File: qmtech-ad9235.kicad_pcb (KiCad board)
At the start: 4 copper layers, 55 x 75 mm, 58 parts

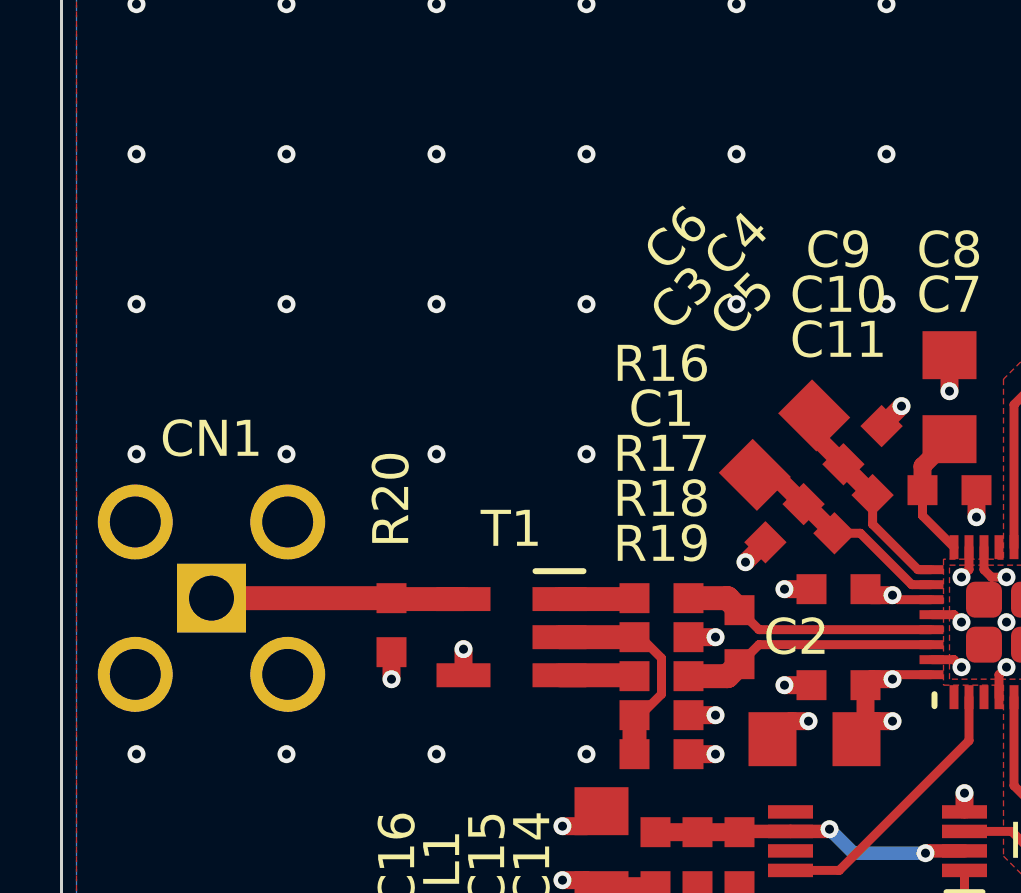
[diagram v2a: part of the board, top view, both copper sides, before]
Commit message: simplify input circuit in qmtech-ad9235
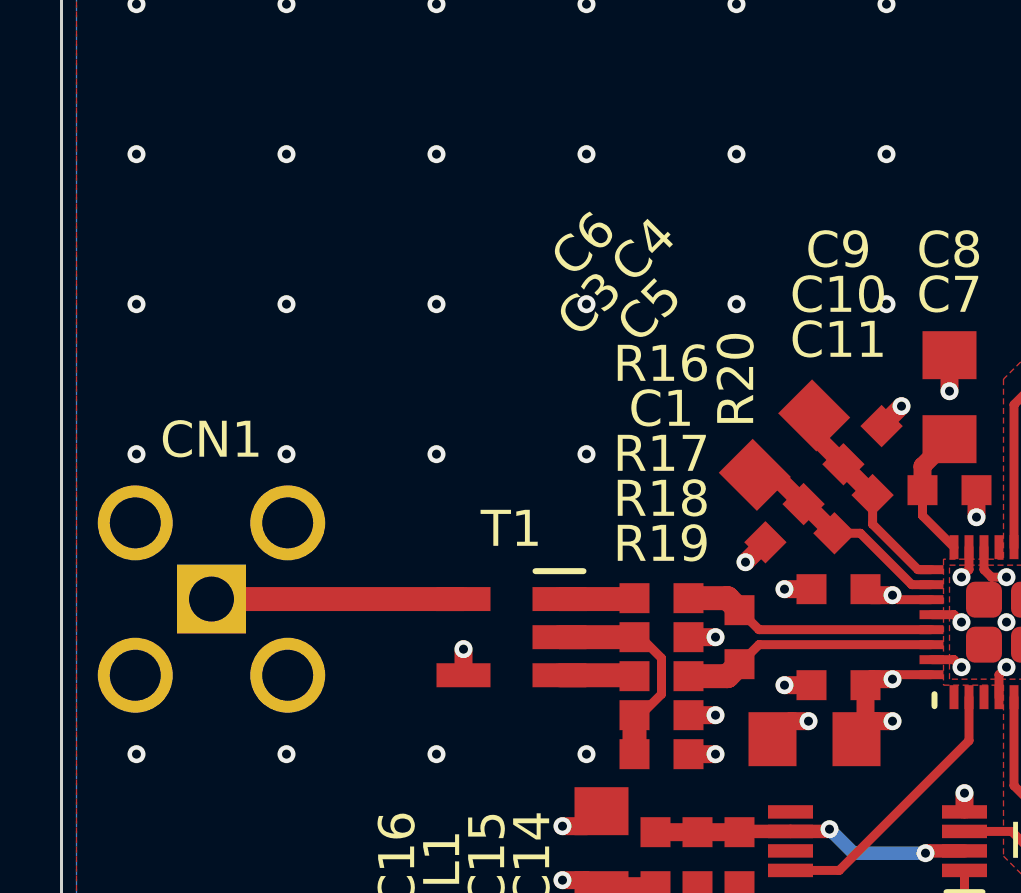
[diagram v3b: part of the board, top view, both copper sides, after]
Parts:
- removed C2: , footprints:0603
- moved R20 11.6 mm to (142.6, 83.6)
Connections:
- R20 pad 1: INPUT -> VIN+
- R20 pad 2: GND -> VIN-
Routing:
- net GND: track 42.1 -> 41.2 mm, vias 138 -> 137
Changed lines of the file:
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@@
     (pad "" np_thru_hole circle (at 0 0) (size 3.2 3.2) (drill 3.2) (layers "*.Cu" "*.Mask"))
-  )
-  (footprint "footprints:0603" (layer "F.Cu")
-    (at 142.6 83.6 -90)
-    (property "mpn" "C1648")
-    (attr smd)
-    (fp_text reference "C2" (at 0 -1.9 -180) (layer "F.SilkS")
-        (effects (font (size 1.2 1.2) (thickness 0.2)))
-    )
-    (fp_text value "" (at 0 0 -90) (layer "F.SilkS")
-        (effects (font (size 1.27 1.27) (thickness 0.15)))
-    )
-    (fp_text user "${REFERENCE}" (at 0 -1.9 -180) (layer "F.Fab")
-        (effects (font (size 1.2 1.2) (thickness 0.2)))
-    )
-    (pad "1" smd rect (at -0.9 0 270) (size 1 1) (layers "F.Cu" "F.Paste" "F.Mask")
-      (net 35 "VIN+"))
-    (pad "2" smd rect (at 0.9 0 270) (size 1 1) (layers "F.Cu" "F.Paste" "F.Mask")
-      (net 36 "VIN-"))
   )
   (footprint "footprints:1206" (layer "F.Cu")
@@
     (property "mpn" "C14663")
     (attr smd)
-    (fp_text reference "C4" (at 1.767768 -7.707463 45) (layer "F.SilkS")
+    (fp_text reference "C4" (at -0.565685 -9.758073 45) (layer "F.SilkS")
         (effects (font (size 1.2 1.2) (thickness 0.2)))
     )
@@
         (effects (font (size 1.27 1.27) (thickness 0.15)))
     )
-    (fp_text user "${REFERENCE}" (at 1.767768 -7.707463 45) (layer "F.Fab")
+    (fp_text user "${REFERENCE}" (at -0.565685 -9.758073 45) (layer "F.Fab")
         (effects (font (size 1.2 1.2) (thickness 0.2)))
     )
@@
   )
   (footprint "footprints:SMA" (layer "F.Cu")
-    (at 125 82.3)
+    (at 125 82.33)
     (property "mpn" "C914554")
     (attr through_hole)
@@
   (footprint "footprints:0603" (layer "F.Cu")
     (at 166.5 105.18)
-    (property "mpn" "C8218")
+    (property "mpn" "C22962")
     (attr smd)
     (fp_text reference "R23" (at -4 0) (layer "F.SilkS")
@@
     (property "mpn" "C14663")
     (attr smd)
-    (fp_text reference "C5" (at 2.333452 -7.566043 45) (layer "F.SilkS")
+    (fp_text reference "C5" (at -0.000001 -9.616653 45) (layer "F.SilkS")
         (effects (font (size 1.2 1.2) (thickness 0.2)))
     )
@@
         (effects (font (size 1.27 1.27) (thickness 0.15)))
     )
-    (fp_text user "${REFERENCE}" (at 2.333452 -7.566043 45) (layer "F.Fab")
+    (fp_text user "${REFERENCE}" (at -0.000001 -9.616653 45) (layer "F.Fab")
         (effects (font (size 1.2 1.2) (thickness 0.2)))
     )
@@
   (footprint "footprints:0603" (layer "F.Cu")
     (at 140 82.3)
-    (property "mpn" "C23140")
+    (property "mpn" "C23345")
     (attr smd)
     (fp_text reference "R16" (at 0 -7.8) (layer "F.SilkS")
@@
     (property "mpn" "C14663")
     (attr smd)
-    (fp_text reference "C3" (at -2.899137 7.707463 -135) (layer "F.SilkS")
+    (fp_text reference "C3" (at -0.565685 9.758073 -135) (layer "F.SilkS")
         (effects (font (size 1.2 1.2) (thickness 0.2)))
     )
@@
         (effects (font (size 1.27 1.27) (thickness 0.15)))
     )
-    (fp_text user "${REFERENCE}" (at -2.899137 7.707463 -135) (layer "F.Fab")
+    (fp_text user "${REFERENCE}" (at -0.565685 9.758073 -135) (layer "F.Fab")
         (effects (font (size 1.2 1.2) (thickness 0.2)))
     )
@@
     (property "mpn" "C13585")
     (attr smd)
-    (fp_text reference "C6" (at 2.333452 -7.424621 45) (layer "F.SilkS")
+    (fp_text reference "C6" (at 0 -9.475231 45) (layer "F.SilkS")
         (effects (font (size 1.2 1.2) (thickness 0.2)))
     )
@@
         (effects (font (size 1.27 1.27) (thickness 0.15)))
     )
-    (fp_text user "${REFERENCE}" (at 2.333452 -7.424621 45) (layer "F.Fab")
+    (fp_text user "${REFERENCE}" (at 0 -9.475231 45) (layer "F.Fab")
         (effects (font (size 1.2 1.2) (thickness 0.2)))
     )
@@
   (footprint "footprints:0603" (layer "F.Cu")
     (at 140 84.9)
-    (property "mpn" "C23140")
+    (property "mpn" "C23345")
     (attr smd)
     (fp_text reference "R17" (at 0 -7.4) (layer "F.SilkS")
@@
   )
   (footprint "footprints:0603" (layer "F.Cu")
-    (at 131 83.2 -90)
-    (property "mpn" "C23185")
-    (attr smd)
-    (fp_text reference "R20" (at -4.2 0 -90) (layer "F.SilkS")
+    (at 142.6 83.6 -90)
+    (property "mpn" "C22962")
+    (attr smd)
+    (fp_text reference "R20" (at -8.6 0.1 90) (layer "F.SilkS")
         (effects (font (size 1.2 1.2) (thickness 0.2)))
     )
@@
         (effects (font (size 1.27 1.27) (thickness 0.15)))
     )
-    (fp_text user "${REFERENCE}" (at -4.2 0 -90) (layer "F.Fab")
+    (fp_text user "${REFERENCE}" (at -8.6 0.1 90) (layer "F.Fab")
         (effects (font (size 1.2 1.2) (thickness 0.2)))
     )
     (pad "1" smd rect (at -0.9 0 270) (size 1 1) (layers "F.Cu" "F.Paste" "F.Mask")
-      (net 40 "INPUT"))
+      (net 35 "VIN+"))
     (pad "2" smd rect (at 0.9 0 270) (size 1 1) (layers "F.Cu" "F.Paste" "F.Mask")
-      (net 18 "GND"))
+      (net 36 "VIN-"))
   )
   (footprint "footprints:SOT23" (layer "F.Cu")
@@
   (footprint "footprints:0603" (layer "F.Cu")
     (at 166.5 110.26)
-    (property "mpn" "C8218")
+    (property "mpn" "C22962")
     (attr smd)
     (fp_text reference "R21" (at -4 0) (layer "F.SilkS")
@@
   (footprint "footprints:0603" (layer "F.Cu")
     (at 166.5 107.72)
-    (property "mpn" "C8218")
+    (property "mpn" "C22962")
     (attr smd)
     (fp_text reference "R22" (at -4 0) (layer "F.SilkS")
@@
   (segment (start 144.1 82) (end 145 82) (width 0.6) (layer "F.Cu") (net 18))
   (segment (start 151.25 85.6) (end 151.25 84.85) (width 0.3) (layer "F.Cu") (net 18))
-  (segment (start 131 85) (end 131 84.1) (width 0.6) (layer "F.Cu") (net 18))
   (segment (start 148 75.9) (end 147.336396 76.563604) (width 0.6) (layer "F.Cu") (net 18))
   (segment (start 133.4 106) (end 133.9 105.5) (width 0.6) (layer "F.Cu") (net 18))
@@
   (via (at 141.8 83.6) (size 0.6) (drill 0.3) (layers "F.Cu" "B.Cu") (free) (net 18))
   (via (at 137.5 127.5) (size 0.6) (drill 0.3) (layers "F.Cu" "B.Cu") (free) (net 18))
-  (via (at 131 85) (size 0.6) (drill 0.3) (layers "F.Cu" "B.Cu") (free) (net 18))
   (via (at 127.5 67.5) (size 0.6) (drill 0.3) (layers "F.Cu" "B.Cu") (free) (net 18))
   (via (at 157.5 127.5) (size 0.6) (drill 0.3) (layers "F.Cu" "B.Cu") (free) (net 18))
@@
   (segment (start 139.07 82.33) (end 139.1 82.3) (width 0.8) (layer "F.Cu") (net 39))
   (segment (start 136.6 82.33) (end 139.07 82.33) (width 0.8) (layer "F.Cu") (net 39))
-  (segment (start 133.4 82.33) (end 131.03 82.33) (width 0.8) (layer "F.Cu") (net 40))
-  (segment (start 125 82.3) (end 131 82.3) (width 0.8) (layer "F.Cu") (net 40))
-  (segment (start 131.03 82.33) (end 131 82.3) (width 0.8) (layer "F.Cu") (net 40))
+  (segment (start 133.4 82.33) (end 125 82.33) (width 0.8) (layer "F.Cu") (net 40))
   (segment (start 143.110051 78.189949) (end 143.762741 78.189949) (width 0.6) (layer "F.Cu") (net 41))
   (segment (start 146.62929 80.136396) (end 145.763604 80.136396) (width 0.3) (layer "F.Cu") (net 41))

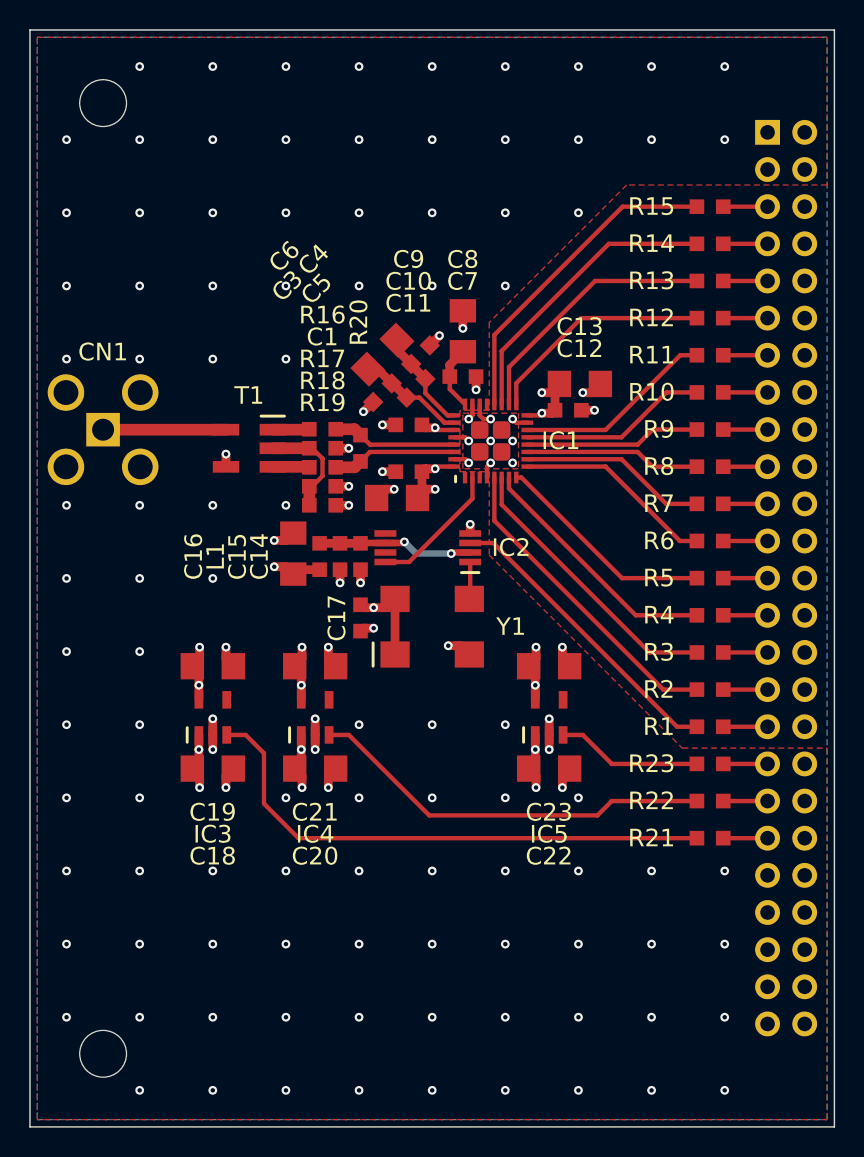
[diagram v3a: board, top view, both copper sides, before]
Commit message: update numbers in capacitor reference designators in qmtech-ad9235
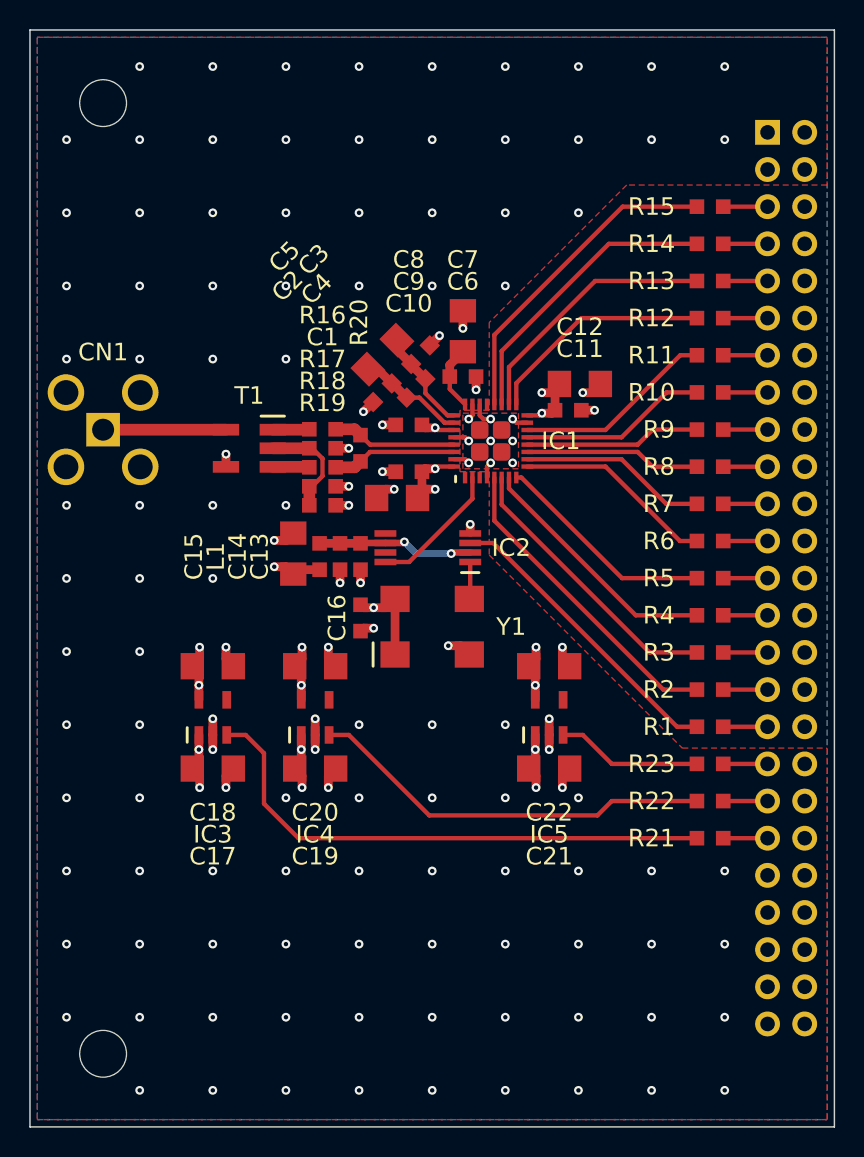
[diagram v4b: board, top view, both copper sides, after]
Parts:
- renumbered C11 to C10, C12 to C11, C13 to C12, C14 to C13, C15 to C14, C16 to C15, C17 to C16, C18 to C17, C19 to C18, C20 to C19, C3 to C2, C21 to C20, C22 to C21, C23 to C22, C4 to C3, C5 to C4, C6 to C5, C7 to C6, C8 to C7, C9 to C8, C10 to C9
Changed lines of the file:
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@@
     (property "mpn" "C14663")
     (attr smd)
-    (fp_text reference "C9" (at 0 11.3) (layer "F.SilkS")
+    (fp_text reference "C8" (at 0 11.3) (layer "F.SilkS")
         (effects (font (size 1.2 1.2) (thickness 0.2)))
     )
@@
     (property "mpn" "C14663")
     (attr smd)
-    (fp_text reference "C17" (at 0 1.6 90) (layer "F.SilkS")
+    (fp_text reference "C16" (at 0 1.6 90) (layer "F.SilkS")
         (effects (font (size 1.2 1.2) (thickness 0.2)))
     )
@@
     (property "mpn" "C13585")
     (attr smd)
-    (fp_text reference "C19" (at 0 10) (layer "F.SilkS")
+    (fp_text reference "C18" (at 0 10) (layer "F.SilkS")
         (effects (font (size 1.2 1.2) (thickness 0.2)))
     )
@@
     (property "mpn" "C14663")
     (attr smd)
-    (fp_text reference "C4" (at -0.565685 -9.758073 45) (layer "F.SilkS")
+    (fp_text reference "C3" (at -0.565685 -9.758073 45) (layer "F.SilkS")
         (effects (font (size 1.2 1.2) (thickness 0.2)))
     )
@@
     (property "mpn" "C13585")
     (attr smd)
-    (fp_text reference "C11" (at -0.8 13.3 180) (layer "F.SilkS")
+    (fp_text reference "C10" (at -0.8 13.3 180) (layer "F.SilkS")
         (effects (font (size 1.2 1.2) (thickness 0.2)))
     )
@@
     (property "mpn" "C14663")
     (attr smd)
-    (fp_text reference "C14" (at 0 6.9 90) (layer "F.SilkS")
+    (fp_text reference "C13" (at 0 6.9 90) (layer "F.SilkS")
         (effects (font (size 1.2 1.2) (thickness 0.2)))
     )
@@
     (property "mpn" "C13585")
     (attr smd)
-    (fp_text reference "C18" (at 0 6) (layer "F.SilkS")
+    (fp_text reference "C17" (at 0 6) (layer "F.SilkS")
         (effects (font (size 1.2 1.2) (thickness 0.2)))
     )
@@
     (property "mpn" "C14663")
     (attr smd)
-    (fp_text reference "C5" (at -0.000001 -9.616653 45) (layer "F.SilkS")
+    (fp_text reference "C4" (at -0.000001 -9.616653 45) (layer "F.SilkS")
         (effects (font (size 1.2 1.2) (thickness 0.2)))
     )
@@
     (property "mpn" "C14663")
     (attr smd)
-    (fp_text reference "C7" (at 0 -6.5) (layer "F.SilkS")
+    (fp_text reference "C6" (at 0 -6.5) (layer "F.SilkS")
         (effects (font (size 1.2 1.2) (thickness 0.2)))
     )
@@
     (property "mpn" "C13585")
     (attr smd)
-    (fp_text reference "C22" (at 0 6) (layer "F.SilkS")
+    (fp_text reference "C21" (at 0 6) (layer "F.SilkS")
         (effects (font (size 1.2 1.2) (thickness 0.2)))
     )
@@
     (property "mpn" "C14663")
     (attr smd)
-    (fp_text reference "C3" (at -0.565685 9.758073 -135) (layer "F.SilkS")
+    (fp_text reference "C2" (at -0.565685 9.758073 -135) (layer "F.SilkS")
         (effects (font (size 1.2 1.2) (thickness 0.2)))
     )
@@
     (property "mpn" "C13585")
     (attr smd)
-    (fp_text reference "C6" (at 0 -9.475231 45) (layer "F.SilkS")
+    (fp_text reference "C5" (at 0 -9.475231 45) (layer "F.SilkS")
         (effects (font (size 1.2 1.2) (thickness 0.2)))
     )
@@
     (property "mpn" "C15849")
     (attr smd)
-    (fp_text reference "C15" (at 0 7 90) (layer "F.SilkS")
+    (fp_text reference "C14" (at 0 7 90) (layer "F.SilkS")
         (effects (font (size 1.2 1.2) (thickness 0.2)))
     )
@@
     (property "mpn" "C14663")
     (attr smd)
-    (fp_text reference "C12" (at 0.8 -4.2) (layer "F.SilkS")
+    (fp_text reference "C11" (at 0.8 -4.2) (layer "F.SilkS")
         (effects (font (size 1.2 1.2) (thickness 0.2)))
     )
@@
     (property "mpn" "C13585")
     (attr smd)
-    (fp_text reference "C20" (at 0 6) (layer "F.SilkS")
+    (fp_text reference "C19" (at 0 6) (layer "F.SilkS")
         (effects (font (size 1.2 1.2) (thickness 0.2)))
     )
@@
     (property "mpn" "C14663")
     (attr smd)
-    (fp_text reference "C10" (at 0 13 180) (layer "F.SilkS")
+    (fp_text reference "C9" (at 0 13 180) (layer "F.SilkS")
         (effects (font (size 1.2 1.2) (thickness 0.2)))
     )
@@
     (property "mpn" "C13585")
     (attr smd)
-    (fp_text reference "C13" (at 0 -3.9) (layer "F.SilkS")
+    (fp_text reference "C12" (at 0 -3.9) (layer "F.SilkS")
         (effects (font (size 1.2 1.2) (thickness 0.2)))
     )
@@
     (property "mpn" "C13585")
     (attr smd)
-    (fp_text reference "C23" (at 0 10) (layer "F.SilkS")
+    (fp_text reference "C22" (at 0 10) (layer "F.SilkS")
         (effects (font (size 1.2 1.2) (thickness 0.2)))
     )
@@
     (property "mpn" "C13585")
     (attr smd)
-    (fp_text reference "C16" (at -0.2 -6.8 90) (layer "F.SilkS")
+    (fp_text reference "C15" (at -0.2 -6.8 90) (layer "F.SilkS")
         (effects (font (size 1.2 1.2) (thickness 0.2)))
     )
@@
     (property "mpn" "C13585")
     (attr smd)
-    (fp_text reference "C8" (at 4.9 0 180) (layer "F.SilkS")
+    (fp_text reference "C7" (at 4.9 0 180) (layer "F.SilkS")
         (effects (font (size 1.2 1.2) (thickness 0.2)))
     )
@@
     (property "mpn" "C13585")
     (attr smd)
-    (fp_text reference "C21" (at 0 10) (layer "F.SilkS")
-        (effects (font (size 1.2 1.2) (thickness 0.2)))
-    )
+    (fp_text reference "C20" (at 0 10) (layer "F.SilkS")
+        (effects (font (size 1.2 1.2) (thickness 0.2)))
+    )
